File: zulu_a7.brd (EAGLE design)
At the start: 61 x 25.4 mm, 177 parts, among them J1 Pmod 2x6, Q1 12MHz 25ppm (FPGA + FT2232HQ), Q3 MBT3904DW1T1, U1 XC7A35T-1CPG236C, U10 93LC46BT-I/SN, U2 FT2232HQ USB-UART/JTAG Bridge, U3 AS4C32M16SB-6TIN, U4 W25Q128JVSIQ, U8 LTC3569EUDC#TRPBF, X1 Molex 105017-0001 Micro-USB-B

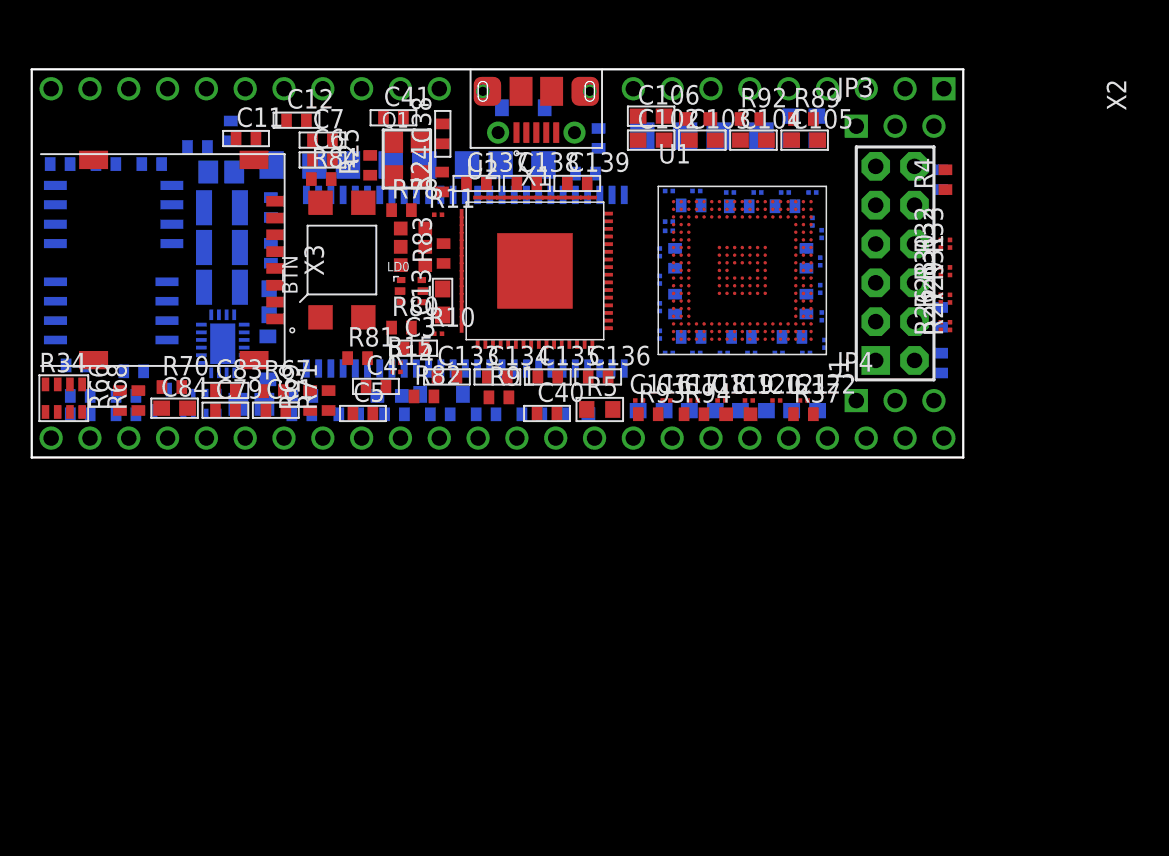
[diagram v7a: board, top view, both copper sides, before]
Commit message: No 1206 left: the bulk becomes twelve 22uF 0805
Each 47uF 1206 splits in two. Nominal per position falls 47 -> 44 uF, but the
0805 is 10 V where the 1206 was 6.3 V, so it derates less under bias and the
pair should deliver at least what the single part did. Height drops 1.60 -> 1.45
mm, which the back-side budget against the 2.54 mm header standoff cares about.
Totals: VCC1V0 6, VCC1V8 2, VCC3V3 4.

The six siblings needed somewhere to be drawn, and every ladder on sheet 7 was
full -- one free slot at x 60.96, and two of the rows reach their rail through a
supply symbol rather than a labelled run. So three new rows go in the empty band
at y 98..151, x 5..30, each with its own rail, GND rail and GND supply
(GND40-42). New segments inside the existing net elements, so they are the same
net by construction and no existing wire moved.

validate.py's UG483 table is updated with them -- it hardcodes counts per rail,
so this was not bookkeeping: 47uF/3/1/2 becomes 22uF/6/2/4.

TWO THINGS THIS TAUGHT ME, BOTH RECORDED WHERE THEY BIT.

Junctions. The rule is cnt + 2*through + (1 if a pin is there) >= 3, so a GND
supply pin with a stub and a rail meeting at it needs a junction even though
only two wires end there. Two were missing and validate named the coordinates.

X3 carries a 0.15 mm CIRCLE on layer 21 at local (4.6, 1.1), and the socket is
rotated R270, which swings that circle out to x 17.20 -- past every wire in the
package. My free-space map read wires and rectangles and not circles, so it
offered C98 a slot at 16.65 that the generator then rejected. The map now reads
circles too.

Two 0805 want more board than one 1206 once each carries its own keepout and
gap, so doubling the count cost area even though every part got smaller: three
of the twelve had no seat, then a fourth fell out when I pinned them. C86, C93,
C97 and C98 are pinned by hand at the REGULATOR, 12.5 to 14.4 mm from U8, which
is where this file already says bulk belongs -- it gains nothing from sitting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
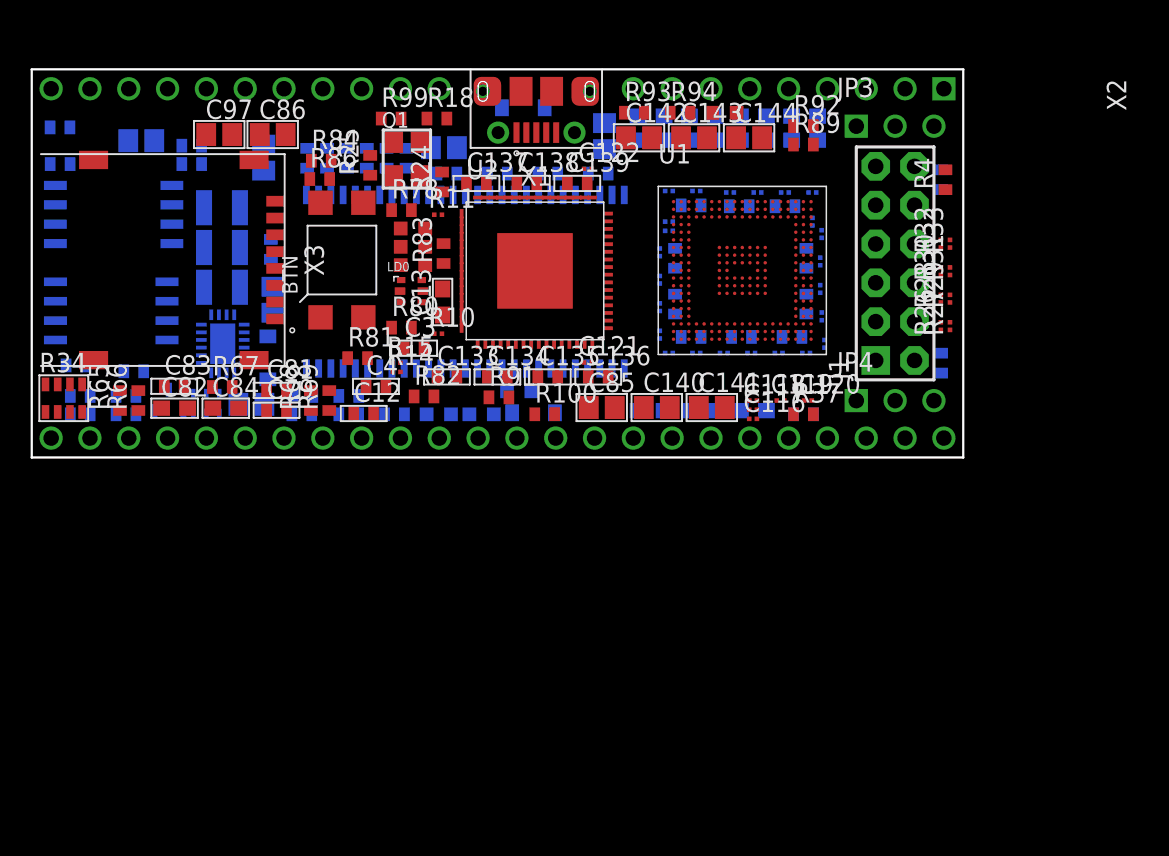
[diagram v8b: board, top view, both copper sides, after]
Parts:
- added C141, C142, C143, C144, C145, C146: 22uF, rcl:C0805
- C140, C85, C86, C93, C97, C98: value 47uF -> 22uF; device rcl:C1206 -> rcl:C0805
- moved C98 34.2 mm to (7.17, 20.7)
- moved C85 25.7 mm to (37.3, 3.27), flipped to the top
- moved L7 21.3 mm to (31.9, 4.33), flipped to the bottom
- moved C122 20.7 mm to (36.4, 18.9)
- moved C101 20.4 mm to (43.9, 22.3)
- moved C100 20.4 mm to (40.5, 22.3)
- moved C106 20.4 mm to (47.2, 3.06), flipped to the bottom
- moved C97 19.9 mm to (12.3, 21.1), flipped to the top
- moved L6 19.8 mm to (45.3, 22.6)
- moved R93 19.8 mm to (39.4, 22.6)
- moved R94 19.8 mm to (42.4, 22.6)
- moved C12 19.7 mm to (21.7, 2.88)
- moved R18 19.6 mm to (26.5, 22.2), flipped to the top
- moved R99 19.6 mm to (23.5, 22.2), flipped to the top
- moved C105 18.9 mm to (43.9, 3.06), flipped to the bottom
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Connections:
- net GND: now also C141.2, C142.2, C143.2, C144.2, C145.2, C146.2
- net VCC1V0: now also C141.1, C142.1, C143.1
- net VCC1V8: now also C144.1
- net VCC3V3: now also C145.1, C146.1
